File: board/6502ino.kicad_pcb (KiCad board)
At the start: 2 copper layers, 53.3 x 53.3 mm, 17 parts, among them U1 W65C02S, U2 IDT71256SA, U3 74HC165, U4 74HC595, U5 74AC00

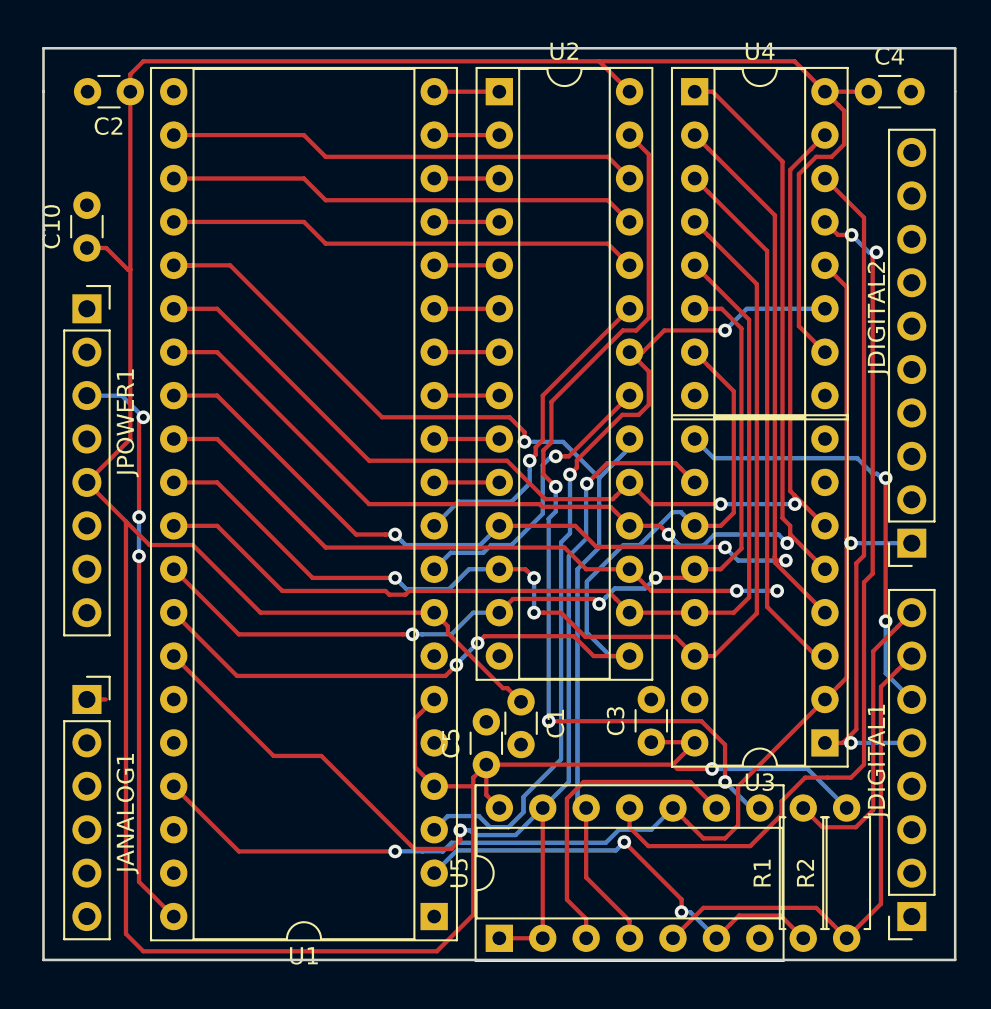
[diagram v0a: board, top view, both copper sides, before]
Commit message: Reduce number of ICs to 3, first working arduino sketch
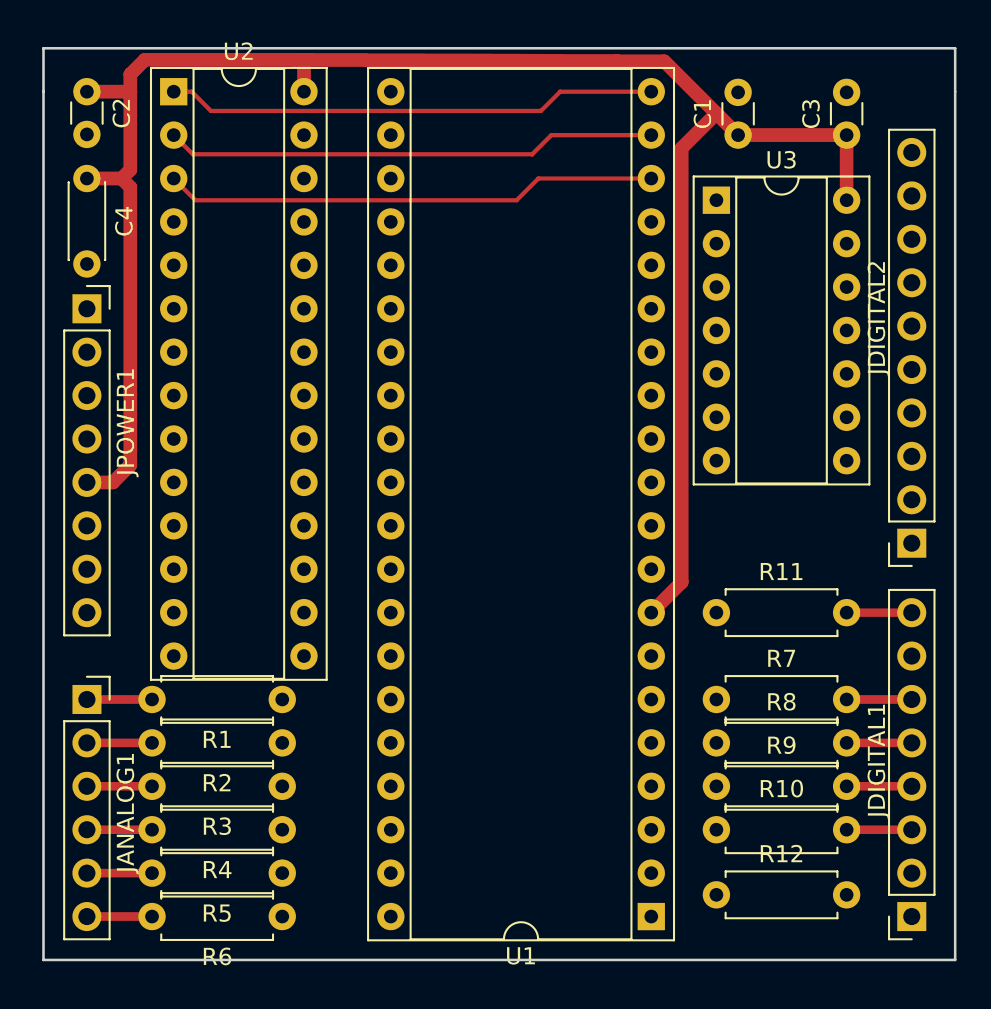
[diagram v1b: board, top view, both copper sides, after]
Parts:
- removed C10: 10uF, Capacitor_THT:C_Disc_D3.0mm_W1.6mm_P2.50mm
- removed C5: 100nF, Capacitor_THT:C_Disc_D3.0mm_W1.6mm_P2.50mm
- removed U4: 74HC595, Package_DIP:DIP-16_W7.62mm_Socket
- removed U5: 74AC00, Package_DIP:DIP-14_W7.62mm_Socket
- added R10: 6K8, Resistor_THT:R_Axial_DIN0207_L6.3mm_D2.5mm_P7.62mm_Horizontal, F.Cu at (176.5, 101.6)
- added R11: 6k8, Resistor_THT:R_Axial_DIN0207_L6.3mm_D2.5mm_P7.62mm_Horizontal, F.Cu at (176.5, 88.9)
- added R12: 100, Resistor_THT:R_Axial_DIN0207_L6.3mm_D2.5mm_P7.62mm_Horizontal, F.Cu at (176.5, 105.4)
- added R3: 6K8, Resistor_THT:R_Axial_DIN0207_L6.3mm_D2.5mm_P7.62mm_Horizontal, F.Cu at (151.1, 99.1)
- added R4: 6K8, Resistor_THT:R_Axial_DIN0207_L6.3mm_D2.5mm_P7.62mm_Horizontal, F.Cu at (151.1, 101.6)
- added R5: 6K8, Resistor_THT:R_Axial_DIN0207_L6.3mm_D2.5mm_P7.62mm_Horizontal, F.Cu at (151.1, 104.1)
- added R6: 6K8, Resistor_THT:R_Axial_DIN0207_L6.3mm_D2.5mm_P7.62mm_Horizontal, F.Cu at (151.1, 106.7)
- added R7: 6K8, Resistor_THT:R_Axial_DIN0207_L6.3mm_D2.5mm_P7.62mm_Horizontal, F.Cu at (176.5, 94.0)
- added R8: 6K8, Resistor_THT:R_Axial_DIN0207_L6.3mm_D2.5mm_P7.62mm_Horizontal, F.Cu at (176.5, 96.5)
- added R9: 6K8, Resistor_THT:R_Axial_DIN0207_L6.3mm_D2.5mm_P7.62mm_Horizontal, F.Cu at (176.5, 99.1)
- C4: value 100nF -> 10uF; footprint Capacitor_THT:C_Disc_D3.0mm_W1.6mm_P2.50mm -> Capacitor_THT:C_Disc_D4.3mm_W1.9mm_P5.00mm
- R1: value 1k -> 6K8
- R2: value 10k -> 6K8
- U3: value 74HC165 -> 74AC00; footprint Package_DIP:DIP-16_W7.62mm_Socket -> Package_DIP:DIP-14_W7.62mm_Socket
- moved C4 46.0 mm to (139.7, 63.5), turned to 270 degrees
- moved C3 37.3 mm to (184.2, 61.0)
- moved C1 35.5 mm to (177.8, 61.0), turned to 90 degrees
- moved R2 34.9 mm to (151.1, 96.5), turned to 180 degrees
- moved R1 33.5 mm to (151.1, 94.0), turned to 180 degrees
- moved U3 32.4 mm to (176.5, 64.8), turned to 0 degrees
- moved U2 19.1 mm to (144.8, 58.4)
- moved U1 12.7 mm to (172.7, 106.7)
- moved C2 2.54 mm to (139.7, 58.4), turned to 270 degrees
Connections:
- JDIGITAL1 pad 5: /IOIN -> Net-(JDIGITAL1-Pad5)
- JDIGITAL1 pad 6: /IOOUT -> Net-(JDIGITAL1-Pad6)
- JDIGITAL1 pad 7: /IOBUSY -> Net-(JDIGITAL1-Pad7)
- JDIGITAL1 pad 8: Net-(JDIGITAL1-Pad8) -> /IOBUSY
- R1 pad 1: /RDY -> /D0
- R1 pad 2: Net-(JDIGITAL1-Pad8) -> Net-(JANALOG1-Pad1)
- R2 pad 1: /IOBUSY -> /D1
- R2 pad 2: +5V -> Net-(JANALOG1-Pad2)
- U1 pad 2: /RDY -> Net-(R12-Pad1)
- U1 pad 3: /PHI1 -> Net-(U1-Pad3)
- U2 pad 22: /PHI1 -> Net-(U2-Pad22)
- U3 pad 1: /IOIN -> /RWB
- U3 pad 10: /RWB -> /PHI2
- U3 pad 11: /D0 -> Net-(U2-Pad22)
- U3 pad 12: /D1 -> /PHI2
- U3 pad 13: /D2 -> /PHI2
- U3 pad 14: /D3 -> +5V
- U3 pad 2: /PHI2 -> /RWB
- U3 pad 3: /D4 -> Net-(U3-Pad3)
- U3 pad 4: /D5 -> /IOBUSY
- U3 pad 5: /D6 -> /IOSELECT
- U3 pad 6: /D7 -> Net-(R12-Pad2)
- U3 pad 7: Net-(U3-Pad7) -> GND
- U3 pad 8: GND -> Net-(U2-Pad27)
- U3 pad 9: /IOOUT -> Net-(U3-Pad3)
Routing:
- net +5V: track 216.2 -> 111.3 mm, vias 1 -> 0
- net /PHI2: track 76.4 -> 0.00 mm, vias 2 -> 0
- net /D6: track 73.4 -> 0.00 mm, vias 2 -> 0
- net /D5: track 72.7 -> 0.00 mm, vias 3 -> 0
- net /D4: track 71.0 -> 0.00 mm, vias 2 -> 0
- net /D7: track 66.9 -> 0.00 mm, vias 2 -> 0
- net /D3: track 65.9 -> 0.00 mm, vias 3 -> 0
- net /RWB: track 65.3 -> 0.00 mm, vias 2 -> 0
- net /IOSELECT: track 63.6 -> 0.00 mm, vias 1 -> 0
- net /D2: track 57.1 -> 0.00 mm
- net /D0: track 57.0 -> 0.00 mm, vias 2 -> 0
- net Net-(U2-Pad27): track 54.0 -> 0.00 mm, vias 3 -> 0
- net /D1: track 53.2 -> 0.00 mm, vias 3 -> 0
- net Net-(U4-Pad13): track 51.8 -> 0.00 mm, vias 2 -> 0
- net /PHI1: track 49.7 -> 0.00 mm, vias 2 -> 0
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
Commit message: Fiddling with the layout
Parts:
- moved C1 24.2 mm to (176.5, 85.1), turned to 0 degrees
- moved C3 20.5 mm to (176.5, 80.0), turned to 0 degrees
- moved U3 13.7 mm to (184.2, 76.2), turned to 180 degrees
- moved R7 2.54 mm to (176.5, 91.4)
- moved R9 2.54 mm to (176.5, 96.5)
- moved R10 2.54 mm to (176.5, 99.1)
- moved R8 2.54 mm to (176.5, 94.0)
- moved R12 1.27 mm to (176.5, 104.1)
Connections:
- R10 pad 2: Net-(JDIGITAL1-Pad3) -> Net-(JDIGITAL1-Pad4)
- R7 pad 2: Net-(JDIGITAL1-Pad6) -> Net-(JDIGITAL1-Pad7)
- R8 pad 2: Net-(JDIGITAL1-Pad5) -> Net-(JDIGITAL1-Pad6)
- R9 pad 2: Net-(JDIGITAL1-Pad4) -> Net-(JDIGITAL1-Pad5)
- U2 pad 10: /A2 -> /A0
- U2 pad 11: /D5 -> /D6
- U2 pad 12: /D3 -> /D4
- U2 pad 13: /D1 -> /D2
- U2 pad 16: /D2 -> /D1
- U2 pad 17: /D4 -> /D3
- U2 pad 18: /D6 -> /D5
- U2 pad 2: /A10 -> /A12
- U2 pad 21: /A0 -> /A3
- U2 pad 23: /A1 -> /A6
- U2 pad 24: /A14 -> /A8
- U2 pad 25: /A13 -> /A9
- U2 pad 26: /A12 -> /A10
- U2 pad 3: /A9 -> /A13
- U2 pad 4: /A8 -> /A14
- U2 pad 6: /A6 -> /A5
- U2 pad 7: /A5 -> /A4
- U2 pad 8: /A4 -> /A2
- U2 pad 9: /A3 -> /A1
- U3 pad 11: Net-(U2-Pad22) -> Net-(R12-Pad2)
- U3 pad 12: /PHI2 -> /IOBUSY
- U3 pad 13: /PHI2 -> /IOSELECT
- U3 pad 4: /IOBUSY -> /PHI2
- U3 pad 5: /IOSELECT -> /PHI2
- U3 pad 6: Net-(R12-Pad2) -> Net-(U2-Pad22)
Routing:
- net /PHI2: track 0.00 -> 74.4 mm, vias 0 -> 2
- net /D6: track 0.00 -> 65.7 mm, vias 0 -> 1
- net /IOSELECT: track 0.00 -> 60.7 mm, vias 0 -> 2
- net /D7: track 0.00 -> 57.5 mm
- net /_RESET: track 0.00 -> 45.2 mm, vias 0 -> 1
- net /RWB: track 0.00 -> 41.6 mm, vias 0 -> 2
- net Net-(R12-Pad2): track 0.00 -> 39.7 mm, vias 0 -> 2
- net /D5: track 0.00 -> 39.1 mm, vias 0 -> 1
- net Net-(U2-Pad22): track 0.00 -> 37.3 mm, vias 0 -> 1
- net /D4: track 0.00 -> 37.2 mm, vias 0 -> 3
- net +5V: track 111.3 -> 143.4 mm
- net /A1: track 0.00 -> 31.2 mm
- net /A2: track 0.00 -> 31.1 mm
- net /A0: track 0.00 -> 31.1 mm
- net /A5: track 0.00 -> 30.0 mm
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
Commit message: PCB layout Rev. 1
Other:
- board text added: "6502ino Rev. 1 github.com/c0pperdragon"
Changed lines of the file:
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@@
   (general
     (thickness 1.6)
-    (drawings 6)
-    (tracks 365)
+    (drawings 7)
+    (tracks 367)
     (zones 0)
     (modules 23)
@@
     (visible_elements 7FFFFFFF)
     (pcbplotparams
-      (layerselection 0x010fc_ffffffff)
+      (layerselection 0x010f0_ffffffff)
       (usegerberextensions false)
       (usegerberattributes false)
@@
       (outputformat 1)
       (mirror false)
-      (drillshape 1)
+      (drillshape 0)
       (scaleselection 1)
-      (outputdirectory ""))
+      (outputdirectory "gerber/"))
   )
   (net 0 "")
@@
     (descr "40-lead though-hole mounted DIP package, row spacing 15.24 mm (600 mils), Socket")
     (tags "THT DIP DIL PDIP 2.54mm 15.24mm 600mil Socket")
-    (fp_text reference U1 (at 7.62 -2.33 180) (layer F.SilkS)
+    (fp_text reference U1 (at -2.54 -1.524 180) (layer F.SilkS)
       (effects (font (size 1 1) (thickness 0.15)))
     )
@@
     (descr "28-lead though-hole mounted DIP package, row spacing 7.62 mm (300 mils), Socket")
     (tags "THT DIP DIL PDIP 2.54mm 7.62mm 300mil Socket")
-    (fp_text reference U2 (at 3.81 -2.33) (layer F.SilkS)
+    (fp_text reference U2 (at -2.54 -1.524) (layer F.SilkS)
       (effects (font (size 1 1) (thickness 0.15)))
     )
@@
     (descr "C, Disc series, Radial, pin pitch=2.50mm, , diameter*width=3.0*1.6mm^2, Capacitor, http://www.vishay.com/docs/45233/krseries.pdf")
     (tags "C Disc series Radial pin pitch 2.50mm  diameter 3.0mm width 1.6mm Capacitor")
-    (fp_text reference C1 (at 1.25 -2.05) (layer F.SilkS)
+    (fp_text reference C1 (at 4.826 0.254) (layer F.SilkS)
       (effects (font (size 1 1) (thickness 0.15)))
     )
@@
     (descr "C, Disc series, Radial, pin pitch=2.50mm, , diameter*width=3.0*1.6mm^2, Capacitor, http://www.vishay.com/docs/45233/krseries.pdf")
     (tags "C Disc series Radial pin pitch 2.50mm  diameter 3.0mm width 1.6mm Capacitor")
-    (fp_text reference C3 (at 1.25 -2.05) (layer F.SilkS)
+    (fp_text reference C3 (at 4.572 0.254) (layer F.SilkS)
       (effects (font (size 1 1) (thickness 0.15)))
     )
@@
     (descr "Resistor, Axial_DIN0207 series, Axial, Horizontal, pin pitch=7.62mm, 0.25W = 1/4W, length*diameter=6.3*2.5mm^2, http://cdn-reichelt.de/documents/datenblatt/B400/1_4W%23YAG.pdf")
     (tags "Resistor Axial_DIN0207 series Axial Horizontal pin pitch 7.62mm 0.25W = 1/4W length 6.3mm diameter 2.5mm")
-    (fp_text reference R1 (at 3.81 -2.37 180) (layer F.SilkS)
+    (fp_text reference R1 (at -2.286 0 180) (layer F.SilkS)
       (effects (font (size 1 1) (thickness 0.15)))
     )
@@
     (descr "Resistor, Axial_DIN0207 series, Axial, Horizontal, pin pitch=7.62mm, 0.25W = 1/4W, length*diameter=6.3*2.5mm^2, http://cdn-reichelt.de/documents/datenblatt/B400/1_4W%23YAG.pdf")
     (tags "Resistor Axial_DIN0207 series Axial Horizontal pin pitch 7.62mm 0.25W = 1/4W length 6.3mm diameter 2.5mm")
-    (fp_text reference R2 (at 3.81 -2.37 180) (layer F.SilkS)
+    (fp_text reference R2 (at -2.286 0 180) (layer F.SilkS)
       (effects (font (size 1 1) (thickness 0.15)))
     )
@@
     (descr "Resistor, Axial_DIN0207 series, Axial, Horizontal, pin pitch=7.62mm, 0.25W = 1/4W, length*diameter=6.3*2.5mm^2, http://cdn-reichelt.de/documents/datenblatt/B400/1_4W%23YAG.pdf")
     (tags "Resistor Axial_DIN0207 series Axial Horizontal pin pitch 7.62mm 0.25W = 1/4W length 6.3mm diameter 2.5mm")
-    (fp_text reference R11 (at 3.81 -2.37) (layer F.SilkS)
+    (fp_text reference R11 (at -1.778 1.27) (layer F.SilkS)
       (effects (font (size 1 1) (thickness 0.15)))
     )
@@
     (descr "Resistor, Axial_DIN0207 series, Axial, Horizontal, pin pitch=7.62mm, 0.25W = 1/4W, length*diameter=6.3*2.5mm^2, http://cdn-reichelt.de/documents/datenblatt/B400/1_4W%23YAG.pdf")
     (tags "Resistor Axial_DIN0207 series Axial Horizontal pin pitch 7.62mm 0.25W = 1/4W length 6.3mm diameter 2.5mm")
-    (fp_text reference R3 (at 3.81 -2.37 180) (layer F.SilkS)
+    (fp_text reference R3 (at -2.286 0 180) (layer F.SilkS)
       (effects (font (size 1 1) (thickness 0.15)))
     )
@@
     (descr "Resistor, Axial_DIN0207 series, Axial, Horizontal, pin pitch=7.62mm, 0.25W = 1/4W, length*diameter=6.3*2.5mm^2, http://cdn-reichelt.de/documents/datenblatt/B400/1_4W%23YAG.pdf")
     (tags "Resistor Axial_DIN0207 series Axial Horizontal pin pitch 7.62mm 0.25W = 1/4W length 6.3mm diameter 2.5mm")
-    (fp_text reference R4 (at 3.81 -2.37 180) (layer F.SilkS)
+    (fp_text reference R4 (at -2.286 0 180) (layer F.SilkS)
       (effects (font (size 1 1) (thickness 0.15)))
     )
@@
     (descr "Resistor, Axial_DIN0207 series, Axial, Horizontal, pin pitch=7.62mm, 0.25W = 1/4W, length*diameter=6.3*2.5mm^2, http://cdn-reichelt.de/documents/datenblatt/B400/1_4W%23YAG.pdf")
     (tags "Resistor Axial_DIN0207 series Axial Horizontal pin pitch 7.62mm 0.25W = 1/4W length 6.3mm diameter 2.5mm")
-    (fp_text reference R5 (at 3.81 -2.37 180) (layer F.SilkS)
+    (fp_text reference R5 (at -2.286 0 180) (layer F.SilkS)
       (effects (font (size 1 1) (thickness 0.15)))
     )
@@
     (descr "Resistor, Axial_DIN0207 series, Axial, Horizontal, pin pitch=7.62mm, 0.25W = 1/4W, length*diameter=6.3*2.5mm^2, http://cdn-reichelt.de/documents/datenblatt/B400/1_4W%23YAG.pdf")
     (tags "Resistor Axial_DIN0207 series Axial Horizontal pin pitch 7.62mm 0.25W = 1/4W length 6.3mm diameter 2.5mm")
-    (fp_text reference R6 (at 3.81 -2.37 180) (layer F.SilkS)
+    (fp_text reference R6 (at -2.286 0 180) (layer F.SilkS)
       (effects (font (size 1 1) (thickness 0.15)))
     )
@@
     (descr "Resistor, Axial_DIN0207 series, Axial, Horizontal, pin pitch=7.62mm, 0.25W = 1/4W, length*diameter=6.3*2.5mm^2, http://cdn-reichelt.de/documents/datenblatt/B400/1_4W%23YAG.pdf")
     (tags "Resistor Axial_DIN0207 series Axial Horizontal pin pitch 7.62mm 0.25W = 1/4W length 6.3mm diameter 2.5mm")
-    (fp_text reference R7 (at 3.81 -2.37) (layer F.SilkS)
+    (fp_text reference R7 (at -1.778 1.27) (layer F.SilkS)
       (effects (font (size 1 1) (thickness 0.15)))
     )
@@
     (descr "Resistor, Axial_DIN0207 series, Axial, Horizontal, pin pitch=7.62mm, 0.25W = 1/4W, length*diameter=6.3*2.5mm^2, http://cdn-reichelt.de/documents/datenblatt/B400/1_4W%23YAG.pdf")
     (tags "Resistor Axial_DIN0207 series Axial Horizontal pin pitch 7.62mm 0.25W = 1/4W length 6.3mm diameter 2.5mm")
-    (fp_text reference R8 (at 3.81 -2.37) (layer F.SilkS)
+    (fp_text reference R8 (at -1.778 1.016) (layer F.SilkS)
       (effects (font (size 1 1) (thickness 0.15)))
     )
@@
     (descr "Resistor, Axial_DIN0207 series, Axial, Horizontal, pin pitch=7.62mm, 0.25W = 1/4W, length*diameter=6.3*2.5mm^2, http://cdn-reichelt.de/documents/datenblatt/B400/1_4W%23YAG.pdf")
     (tags "Resistor Axial_DIN0207 series Axial Horizontal pin pitch 7.62mm 0.25W = 1/4W length 6.3mm diameter 2.5mm")
-    (fp_text reference R9 (at 3.81 -2.37) (layer F.SilkS)
+    (fp_text reference R9 (at -1.778 1.016) (layer F.SilkS)
       (effects (font (size 1 1) (thickness 0.15)))
     )
@@
     (descr "Resistor, Axial_DIN0207 series, Axial, Horizontal, pin pitch=7.62mm, 0.25W = 1/4W, length*diameter=6.3*2.5mm^2, http://cdn-reichelt.de/documents/datenblatt/B400/1_4W%23YAG.pdf")
     (tags "Resistor Axial_DIN0207 series Axial Horizontal pin pitch 7.62mm 0.25W = 1/4W length 6.3mm diameter 2.5mm")
-    (fp_text reference R10 (at 3.81 -2.37) (layer F.SilkS)
+    (fp_text reference R10 (at -1.27 1.778) (layer F.SilkS)
       (effects (font (size 1 1) (thickness 0.15)))
     )
@@
     (descr "Resistor, Axial_DIN0207 series, Axial, Horizontal, pin pitch=7.62mm, 0.25W = 1/4W, length*diameter=6.3*2.5mm^2, http://cdn-reichelt.de/documents/datenblatt/B400/1_4W%23YAG.pdf")
     (tags "Resistor Axial_DIN0207 series Axial Horizontal pin pitch 7.62mm 0.25W = 1/4W length 6.3mm diameter 2.5mm")
-    (fp_text reference R12 (at 3.81 -2.37) (layer F.SilkS)
+    (fp_text reference R12 (at -1.27 1.778) (layer F.SilkS)
       (effects (font (size 1 1) (thickness 0.15)))
     )
@@
       (rotate (xyz 0 0 0))
     )
+  )
+  (gr_text "6502ino Rev. 1\ngithub.com/c0pperdragon" (at 164.846 84.074 90) (layer B.SilkS)
+    (effects (font (size 1.5 1.5) (thickness 0.3)) (justify mirror))
   )
   (gr_line (start 190.5 109.22) (end 137.16 109.22) (layer Edge.Cuts) (width 0.15))
@@
   (segment (start 184.15 83.82) (end 184.15 83.312) (width 0.25) (layer F.Cu) (net 49))
   (segment (start 158.279999 99.859999) (end 157.48 99.06) (width 0.25) (layer F.Cu) (net 49))
+  (segment (start 158.75 100.33) (end 158.279999 99.859999) (width 0.25) (layer F.Cu) (net 49))
+  (segment (start 178.816 100.33) (end 158.75 100.33) (width 0.25) (layer F.Cu) (net 49))
+  (segment (start 182.118 85.09) (end 182.118 90.678) (width 0.25) (layer F.Cu) (net 49))
+  (segment (start 182.118 90.678) (end 179.832 92.964) (width 0.25) (layer F.Cu) (net 49))
+  (segment (start 179.832 92.964) (end 179.832 99.314) (width 0.25) (layer F.Cu) (net 49))
+  (segment (start 182.88 84.328) (end 182.118 85.09) (width 0.25) (layer F.Cu) (net 49))
   (segment (start 184.15 84.328) (end 182.88 84.328) (width 0.25) (layer F.Cu) (net 49))
-  (segment (start 182.118 85.09) (end 182.118 96.52) (width 0.25) (layer F.Cu) (net 49))
-  (segment (start 182.118 96.52) (end 178.308 100.33) (width 0.25) (layer F.Cu) (net 49))
-  (segment (start 178.308 100.33) (end 158.75 100.33) (width 0.25) (layer F.Cu) (net 49))
-  (segment (start 182.88 84.328) (end 182.118 85.09) (width 0.25) (layer F.Cu) (net 49))
-  (segment (start 158.75 100.33) (end 158.279999 99.859999) (width 0.25) (layer F.Cu) (net 49))
+  (segment (start 179.832 99.314) (end 178.816 100.33) (width 0.25) (layer F.Cu) (net 49))
   (segment (start 184.15 88.9) (end 187.96 88.9) (width 0.5) (layer F.Cu) (net 50))
   (via (at 180.34 71.628) (size 0.8) (drill 0.4) (layers F.Cu B.Cu) (net 50))

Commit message: Fix: Connect BE to +5V
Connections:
- U1 pad 36: Net-(U1-Pad36) -> +5V
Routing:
- net +5V: track 143.4 -> 156.9 mm
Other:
- board text added: "6502ino Rev. 2 github.com/c0pperdragon"
- board text removed: "6502ino Rev. 1 github.com/c0pperdragon"
